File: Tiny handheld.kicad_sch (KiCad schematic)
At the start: 38 parts, among them J1 Conn_01x04_Female, J2 Conn_01x04_Female, J3 TYPE-C-31-M-12, U1 ATtiny85-20P, U2 ATtiny85-20M, U3 EEPROM-I2CEIAJ

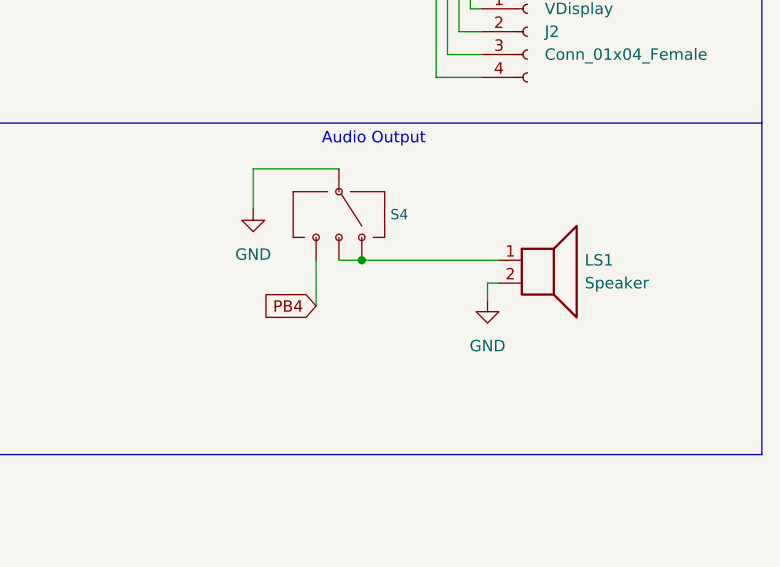
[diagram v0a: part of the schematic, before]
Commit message: changed switch for audio toggle
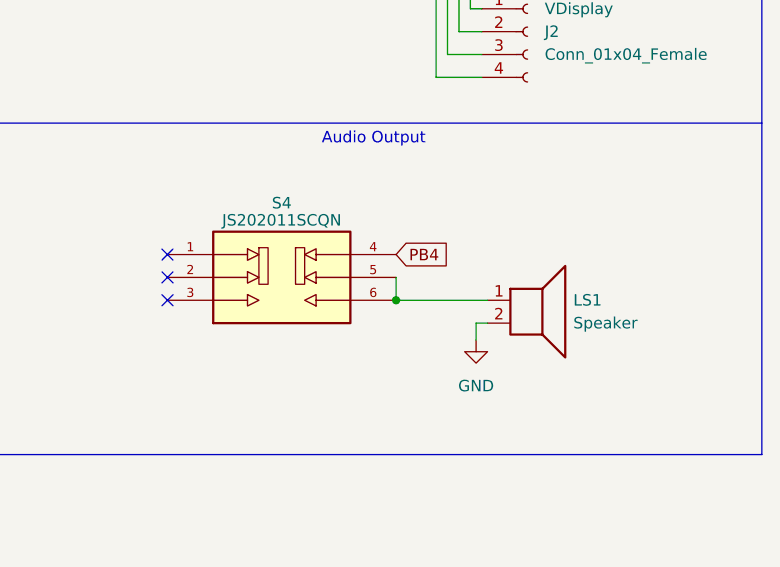
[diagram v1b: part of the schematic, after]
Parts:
- removed S4: SWITCH-SP3T-SMD, Snapeda:SW_JS202011SCQN, symbol SparkFun-Switches:SWITCH-SP3T-SMD
- added S4: JS202011SCQN, Snapeda:SW_JS202011SCQN, symbol JS202011SCQN:JS202011SCQN
- S3: footprint SnapEDA Library:SW_JS202011SCQN -> Snapeda:SW_JS202011SCQN
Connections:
- net PB4: now also S4.4
- net at LS1.1: now also S4.5, S4.6
- no-connect marks 2 -> 5
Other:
- moved on the sheet: LS1

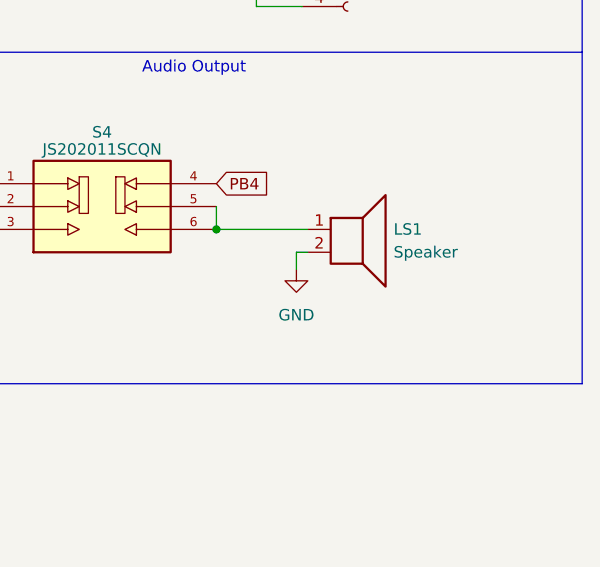
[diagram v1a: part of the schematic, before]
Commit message: changed speaker footprint and updated it
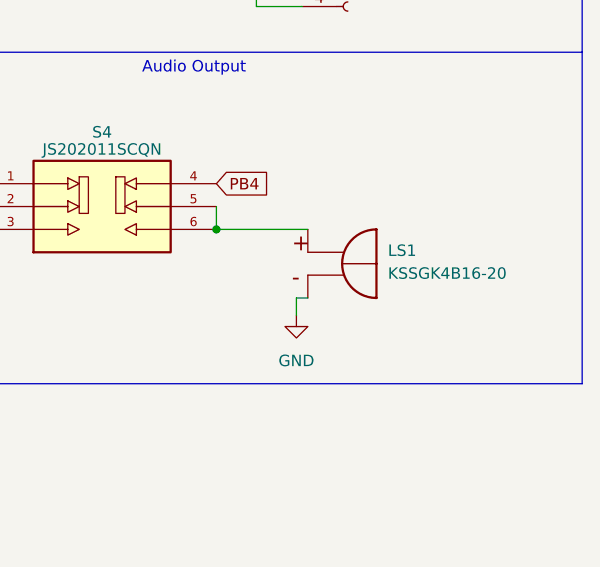
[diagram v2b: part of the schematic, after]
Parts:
- removed LS1: Speaker, Connector_PinHeader_2.54mm:PinHeader_1x02_P2.54mm_Vertical, symbol Device:Speaker
- added LS1: KSSGK4B16-20, Snapeda:XDCR_KSSGK4B16-20, symbol KSSGK4B16-20:KSSGK4B16-20
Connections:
- net GND: now also LS1.N
- net at S4.5, S4.6: now also LS1.P
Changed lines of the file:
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@@
     (stroke (width 0) (type default) (color 0 0 0 0))
   )
-  (wire (pts (xy 250.19 74.93) (xy 250.19 76.835))
+  (wire (pts (xy 250.19 80.01) (xy 250.19 81.915))
     (stroke (width 0) (type default) (color 0 0 0 0))
   )
@@
     (stroke (width 0) (type default) (color 0 0 0 0))
   )
-  (wire (pts (xy 251.46 74.93) (xy 250.19 74.93))
+  (wire (pts (xy 251.46 80.01) (xy 250.19 80.01))
     (stroke (width 0) (type default) (color 0 0 0 0))
   )
@@
     (pin "2")
   )
-  (symbol (lib_id "Device:Speaker") (at 256.54 72.39 0) (unit 1)
-    (in_bom yes) (on_board yes) (fields_autoplaced)
-    (property "Reference" "LS1" (id 0) (at 260.985 72.3899 0)
-      (effects (font (size 1.27 1.27)) (justify left))
-    )
-    (property "Value" "Speaker" (id 1) (at 260.985 74.9299 0)
-      (effects (font (size 1.27 1.27)) (justify left))
-    )
-    (property "Footprint" "Connector_PinHeader_2.54mm:PinHeader_1x02_P2.54mm_Vertical" (id 2) (at 256.54 77.47 0)
-      (effects (font (size 1.27 1.27)) hide)
-    )
-    (property "Datasheet" "~" (id 3) (at 256.286 73.66 0)
-      (effects (font (size 1.27 1.27)) hide)
-    )
-    (pin "1")
-    (pin "2")
-  )
   (symbol (lib_id "Device:D_Schottky") (at 50.8 100.33 180) (unit 1)
     (in_bom yes) (on_board yes)
@@
     (pin "4")
   )
-  (symbol (lib_id "power:GND") (at 250.19 76.835 0) (unit 1)
-    (in_bom yes) (on_board yes) (fields_autoplaced)
-    (property "Reference" "#PWR0110" (id 0) (at 250.19 83.185 0)
-      (effects (font (size 1.27 1.27)) hide)
-    )
-    (property "Value" "GND" (id 1) (at 250.19 81.915 0))
-    (property "Footprint" "" (id 2) (at 250.19 76.835 0)
-      (effects (font (size 1.27 1.27)) hide)
-    )
-    (property "Datasheet" "" (id 3) (at 250.19 76.835 0)
+  (symbol (lib_id "power:GND") (at 250.19 81.915 0) (unit 1)
+    (in_bom yes) (on_board yes) (fields_autoplaced)
+    (property "Reference" "#PWR0110" (id 0) (at 250.19 88.265 0)
+      (effects (font (size 1.27 1.27)) hide)
+    )
+    (property "Value" "GND" (id 1) (at 250.19 86.995 0))
+    (property "Footprint" "" (id 2) (at 250.19 81.915 0)
+      (effects (font (size 1.27 1.27)) hide)
+    )
+    (property "Datasheet" "" (id 3) (at 250.19 81.915 0)
       (effects (font (size 1.27 1.27)) hide)
     )
@@
     (pin "1")
   )
+  (symbol (lib_id "KSSGK4B16-20:KSSGK4B16-20") (at 254 77.47 0) (unit 1)
+    (in_bom yes) (on_board yes) (fields_autoplaced)
+    (property "Reference" "LS1" (id 0) (at 260.35 74.7487 0)
+      (effects (font (size 1.27 1.27)) (justify left))
+    )
+    (property "Value" "KSSGK4B16-20" (id 1) (at 260.35 77.2887 0)
+      (effects (font (size 1.27 1.27)) (justify left))
+    )
+    (property "Footprint" "Snapeda:XDCR_KSSGK4B16-20" (id 2) (at 254 77.47 0)
+      (effects (font (size 1.27 1.27)) (justify left bottom) hide)
+    )
+    (property "Datasheet" "" (id 3) (at 254 77.47 0)
+      (effects (font (size 1.27 1.27)) (justify left bottom) hide)
+    )
+    (property "STANDARD" "Manufacturer recommendations" (id 4) (at 254 77.47 0)
+      (effects (font (size 1.27 1.27)) (justify left bottom) hide)
+    )
+    (property "MAXIMUM_PACKAGE_HEIGHT" "2.2 mm" (id 5) (at 254 77.47 0)
+      (effects (font (size 1.27 1.27)) (justify left bottom) hide)
+    )
+    (property "MANUFACTURER" "Kingstate" (id 6) (at 254 77.47 0)
+      (effects (font (size 1.27 1.27)) (justify left bottom) hide)
+    )
+    (property "PARTREV" "1.1" (id 7) (at 254 77.47 0)
+      (effects (font (size 1.27 1.27)) (justify left bottom) hide)
+    )
+    (pin "N")
+    (pin "P")
+  )
   (symbol (lib_id "Device:C") (at 106.68 73.025 0) (unit 1)
     (in_bom yes) (on_board yes) (fields_autoplaced)
@@
       (reference "JP4") (unit 1) (value "SolderJumper_3_Bridged123") (footprint "Jumper:SolderJumper-3_P1.3mm_Open_RoundedPad1.0x1.5mm_NumberLabels")
     )
-    (path "/67918cda-4e84-4d93-8647-d5f18ad30e68"
-      (reference "LS1") (unit 1) (value "Speaker") (footprint "Connector_PinHeader_2.54mm:PinHeader_1x02_P2.54mm_Vertical")
+    (path "/e6505e47-bcf4-4c11-974c-950bd16fce03"
+      (reference "LS1") (unit 1) (value "KSSGK4B16-20") (footprint "Snapeda:XDCR_KSSGK4B16-20")
     )
     (path "/b3cf5acc-e257-462d-850a-8059d86079a1"

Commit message: first layout tryout
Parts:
- D1, D2, D3: footprint Diode_SMD:D_3220_8050Metric_Pad2.65x5.15mm_HandSolder -> Diode_SMD:D_1210_3225Metric_Pad1.42x2.65mm_HandSolder
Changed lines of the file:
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@@
       (effects (font (size 1.27 1.27)) (justify left))
     )
-    (property "Footprint" "Diode_SMD:D_3220_8050Metric_Pad2.65x5.15mm_HandSolder" (id 2) (at 56.515 134.62 0)
+    (property "Footprint" "Diode_SMD:D_1210_3225Metric_Pad1.42x2.65mm_HandSolder" (id 2) (at 56.515 134.62 0)
       (effects (font (size 1.27 1.27)) hide)
     )
@@
       (effects (font (size 1.27 1.27)) (justify left))
     )
-    (property "Footprint" "Diode_SMD:D_3220_8050Metric_Pad2.65x5.15mm_HandSolder" (id 2) (at 48.895 134.62 0)
+    (property "Footprint" "Diode_SMD:D_1210_3225Metric_Pad1.42x2.65mm_HandSolder" (id 2) (at 48.895 134.62 0)
       (effects (font (size 1.27 1.27)) hide)
     )
@@
     (property "Reference" "D1" (id 0) (at 50.8 102.87 0))
     (property "Value" "D_Schottky" (id 1) (at 53.975 97.155 0))
-    (property "Footprint" "Diode_SMD:D_3220_8050Metric_Pad2.65x5.15mm_HandSolder" (id 2) (at 50.8 100.33 0)
+    (property "Footprint" "Diode_SMD:D_1210_3225Metric_Pad1.42x2.65mm_HandSolder" (id 2) (at 50.8 100.33 0)
       (effects (font (size 1.27 1.27)) hide)
     )
@@
     )
     (path "/68f90c2a-7c7b-4d9c-8790-32721f4e1926"
-      (reference "D1") (unit 1) (value "D_Schottky") (footprint "Diode_SMD:D_3220_8050Metric_Pad2.65x5.15mm_HandSolder")
+      (reference "D1") (unit 1) (value "D_Schottky") (footprint "Diode_SMD:D_1210_3225Metric_Pad1.42x2.65mm_HandSolder")
     )
     (path "/5fd767ee-7166-48a9-a790-5eaffbe151cb"
-      (reference "D2") (unit 1) (value "3.6V") (footprint "Diode_SMD:D_3220_8050Metric_Pad2.65x5.15mm_HandSolder")
+      (reference "D2") (unit 1) (value "3.6V") (footprint "Diode_SMD:D_1210_3225Metric_Pad1.42x2.65mm_HandSolder")
     )
     (path "/3e1cd6ec-9057-4025-a95a-6564cb6c9ca0"
-      (reference "D3") (unit 1) (value "3.6V") (footprint "Diode_SMD:D_3220_8050Metric_Pad2.65x5.15mm_HandSolder")
+      (reference "D3") (unit 1) (value "3.6V") (footprint "Diode_SMD:D_1210_3225Metric_Pad1.42x2.65mm_HandSolder")
     )
     (path "/c820fea6-c141-491b-a697-ecc854c32ead"

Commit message: updated schematic (nothing special)
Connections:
- net PB0/SDA/MOSI: now also U1.5 (AREF/PB0), U2.11 (AREF/PB0)
- net PB1/MISO: now also U1.6 (PB1), U2.12 (PB1)
- net PB2/SCL/SCK: now also U1.7 (PB2), U2.14 (PB2)
- net PB3: now also U1.2 (XTAL1/PB3), U2.2 (XTAL1/PB3)
- net PB4: now also U1.3 (XTAL2/PB4), U2.5 (XTAL2/PB4)
- net PB5/RES: now also U1.1 (~{RESET}/PB5), U2.1 (~{RESET}/PB5)
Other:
- moved on the sheet: U1, U2
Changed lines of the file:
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@@
   (junction (at 43.18 83.185) (diameter 0) (color 0 0 0 0)
   )
-  (junction (at 160.655 35.56) (diameter 0) (color 0 0 0 0)
+  (junction (at 160.655 29.845) (diameter 0) (color 0 0 0 0)
+  )
+  (junction (at 160.655 34.925) (diameter 0) (color 0 0 0 0)
+  )
+  (junction (at 130.175 34.925) (diameter 0) (color 0 0 0 0)
   )
   (junction (at 53.34 83.185) (diameter 0) (color 0 0 0 0)
@@
   (junction (at 245.745 34.925) (diameter 0) (color 0 0 0 0)
   )
+  (junction (at 130.175 29.845) (diameter 0) (color 0 0 0 0)
+  )
   (junction (at 132.715 64.77) (diameter 0) (color 0 0 0 0)
   )
-  (junction (at 130.175 35.56) (diameter 0) (color 0 0 0 0)
-  )
   (junction (at 43.18 106.68) (diameter 0) (color 0 0 0 0)
   )
@@
   (junction (at 132.715 52.07) (diameter 0) (color 0 0 0 0)
   )
+  (junction (at 130.175 27.305) (diameter 0) (color 0 0 0 0)
+  )
   (junction (at 48.895 128.905) (diameter 0) (color 0 0 0 0)
   )
@@
   (junction (at 29.845 134.62) (diameter 0) (color 0 0 0 0)
   )
+  (junction (at 160.655 27.305) (diameter 0) (color 0 0 0 0)
+  )
   (junction (at 42.545 116.84) (diameter 0) (color 0 0 0 0)
   )
@@
   (junction (at 164.465 32.385) (diameter 0) (color 0 0 0 0)
   )
-  (junction (at 128.905 107.315) (diameter 0) (color 0 0 0 0)
+  (junction (at 160.655 32.385) (diameter 0) (color 0 0 0 0)
   )
   (junction (at 160.655 49.53) (diameter 0) (color 0 0 0 0)
@@
   (junction (at 53.34 50.165) (diameter 0) (color 0 0 0 0)
   )
-  (junction (at 36.83 22.225) (diameter 0) (color 0 0 0 0)
-  )
   (junction (at 42.545 114.3) (diameter 0) (color 0 0 0 0)
   )
@@
   )
   (junction (at 247.015 32.385) (diameter 0) (color 0 0 0 0)
+  )
+  (junction (at 130.175 32.385) (diameter 0) (color 0 0 0 0)
   )
   (junction (at 132.715 49.53) (diameter 0) (color 0 0 0 0)
@@
     (stroke (width 0) (type default) (color 0 0 0 0))
   )
-  (wire (pts (xy 160.655 35.56) (xy 160.655 43.18))
+  (wire (pts (xy 160.655 34.925) (xy 160.655 43.18))
     (stroke (width 0) (type default) (color 0 0 0 0))
   )
@@
     (stroke (width 0) (type default) (color 0 0 0 0))
   )
-  (wire (pts (xy 130.175 35.56) (xy 130.175 45.72))
+  (wire (pts (xy 130.175 34.925) (xy 130.175 45.72))
     (stroke (width 0) (type default) (color 0 0 0 0))
   )
@@
     (stroke (width 0) (type default) (color 0 0 0 0))
   )
-  (wire (pts (xy 160.655 34.925) (xy 160.655 35.56))
-    (stroke (width 0) (type default) (color 0 0 0 0))
-  )
   (wire (pts (xy 165.735 64.77) (xy 167.005 64.77))
     (stroke (width 0) (type default) (color 0 0 0 0))
@@
   )
   (wire (pts (xy 97.155 113.665) (xy 97.155 107.315))
-    (stroke (width 0) (type default) (color 0 0 0 0))
-  )
-  (wire (pts (xy 130.175 34.925) (xy 130.175 35.56))
     (stroke (width 0) (type default) (color 0 0 0 0))
   )
@@
     )
   )
+  (global_label "VCC" (shape input) (at 36.83 22.225 90) (fields_autoplaced)
+    (effects (font (size 1.27 1.27)) (justify left))
+    (property "Intersheet References" "${INTERSHEET_REFS}" (id 0) (at 36.7506 16.1833 90)
+      (effects (font (size 1.27 1.27)) (justify left) hide)
+    )
+  )
   (global_label "PB5{slash}RES" (shape input) (at 118.745 27.305 180) (fields_autoplaced)
     (effects (font (size 1.27 1.27)) (justify right))
@@
     (effects (font (size 1.27 1.27)) (justify left))
     (property "Intersheet References" "${INTERSHEET_REFS}" (id 0) (at 84.9026 34.8456 0)
+      (effects (font (size 1.27 1.27)) (justify left) hide)
+    )
+  )
+  (global_label "VCC" (shape input) (at 128.905 107.315 0) (fields_autoplaced)
+    (effects (font (size 1.27 1.27)) (justify left))
+    (property "Intersheet References" "${INTERSHEET_REFS}" (id 0) (at 134.9467 107.2356 0)
       (effects (font (size 1.27 1.27)) (justify left) hide)
     )
@@
     (pin "2")
   )
-  (symbol (lib_id "MCU_Microchip_ATtiny:ATtiny85-20P") (at 145.415 34.29 0) (unit 1)
-    (in_bom yes) (on_board yes)
-    (property "Reference" "U1" (id 0) (at 140.97 22.225 0)
+  (symbol (lib_id "MCU_Microchip_ATtiny:ATtiny85-20P") (at 145.415 33.655 0) (unit 1)
+    (in_bom yes) (on_board yes)
+    (property "Reference" "U1" (id 0) (at 140.97 21.59 0)
       (effects (font (size 1.27 1.27)) (justify right))
     )
-    (property "Value" "ATtiny85-20P" (id 1) (at 144.78 24.13 0)
+    (property "Value" "ATtiny85-20P" (id 1) (at 144.78 23.495 0)
       (effects (font (size 1.27 1.27)) (justify right))
     )
-    (property "Footprint" "Package_DIP:DIP-8_W7.62mm" (id 2) (at 147.32 62.23 0)
+    (property "Footprint" "Package_DIP:DIP-8_W7.62mm" (id 2) (at 147.32 61.595 0)
       (effects (font (size 1.27 1.27) italic) hide)
     )
-    (property "Datasheet" "http://ww1.microchip.com/downloads/en/DeviceDoc/atmel-2586-avr-8-bit-microcontroller-attiny25-attiny45-attiny85_datasheet.pdf" (id 3) (at 160.02 58.42 0)
+    (property "Datasheet" "http://ww1.microchip.com/downloads/en/DeviceDoc/atmel-2586-avr-8-bit-microcontroller-attiny25-attiny45-attiny85_datasheet.pdf" (id 3) (at 160.02 57.785 0)
       (effects (font (size 1.27 1.27)) hide)
     )
@@
     (pin "1")
   )
-  (symbol (lib_id "power:VCC") (at 128.905 107.315 0) (unit 1)
-    (in_bom yes) (on_board yes) (fields_autoplaced)
-    (property "Reference" "#PWR0105" (id 0) (at 128.905 111.125 0)
-      (effects (font (size 1.27 1.27)) hide)
-    )
-    (property "Value" "VCC" (id 1) (at 128.905 102.235 0))
-    (property "Footprint" "" (id 2) (at 128.905 107.315 0)
-      (effects (font (size 1.27 1.27)) hide)
-    )
-    (property "Datasheet" "" (id 3) (at 128.905 107.315 0)
-      (effects (font (size 1.27 1.27)) hide)
-    )
-    (pin "1")
-  )
   (symbol (lib_id "Device:R") (at 43.18 53.975 0) (unit 1)
     (in_bom yes) (on_board yes) (fields_autoplaced)
@@
     (pin "2")
   )
-  (symbol (lib_id "power:VCC") (at 36.83 22.225 0) (unit 1)
-    (in_bom yes) (on_board yes) (fields_autoplaced)
-    (property "Reference" "#PWR0109" (id 0) (at 36.83 26.035 0)
-      (effects (font (size 1.27 1.27)) hide)
-    )
-    (property "Value" "VCC" (id 1) (at 36.83 17.145 0))
-    (property "Footprint" "" (id 2) (at 36.83 22.225 0)
-      (effects (font (size 1.27 1.27)) hide)
-    )
-    (property "Datasheet" "" (id 3) (at 36.83 22.225 0)
-      (effects (font (size 1.27 1.27)) hide)
-    )
-    (pin "1")
-  )
   (symbol (lib_id "power:PWR_FLAG") (at 43.18 106.68 0) (unit 1)
     (in_bom yes) (on_board yes) (fields_autoplaced)
@@
     (pin "4")
   )
-  (symbol (lib_id "MCU_Microchip_ATtiny:ATtiny85-20M") (at 145.415 41.91 0) (unit 1)
-    (in_bom yes) (on_board yes)
-    (property "Reference" "U2" (id 0) (at 153.035 22.225 0)
+  (symbol (lib_id "MCU_Microchip_ATtiny:ATtiny85-20M") (at 145.415 41.275 0) (unit 1)
+    (in_bom yes) (on_board yes)
+    (property "Reference" "U2" (id 0) (at 153.035 21.59 0)
       (effects (font (size 1.27 1.27)) (justify right))
     )
-    (property "Value" "ATtiny85-20M" (id 1) (at 161.29 24.13 0)
+    (property "Value" "ATtiny85-20M" (id 1) (at 161.29 23.495 0)
       (effects (font (size 1.27 1.27)) (justify right))
     )
-    (property "Footprint" "Snapeda:QFN50P400X400X80-21N" (id 2) (at 156.21 45.085 0)
+    (property "Footprint" "Snapeda:QFN50P400X400X80-21N" (id 2) (at 156.21 44.45 0)
       (effects (font (size 1.27 1.27) italic) hide)
     )
-    (property "Datasheet" "http://ww1.microchip.com/downloads/en/DeviceDoc/atmel-2586-avr-8-bit-microcontroller-attiny25-attiny45-attiny85_datasheet.pdf" (id 3) (at 186.055 42.545 0)
+    (property "Datasheet" "http://ww1.microchip.com/downloads/en/DeviceDoc/atmel-2586-avr-8-bit-microcontroller-attiny25-attiny45-attiny85_datasheet.pdf" (id 3) (at 186.055 41.91 0)
       (effects (font (size 1.27 1.27)) hide)
     )
@@
       (reference "#PWR0104") (unit 1) (value "GND") (footprint "")
     )
-    (path "/8f597b01-b914-42f9-803c-9063988abc27"
-      (reference "#PWR0105") (unit 1) (value "VCC") (footprint "")
-    )
     (path "/ef165256-f975-442e-8a79-6b8715d4b315"
       (reference "#PWR0106") (unit 1) (value "GND") (footprint "")
@@
       (reference "#PWR0108") (unit 1) (value "VCC") (footprint "")
     )
-    (path "/b7b686cb-da0a-46af-a6c0-01b14bd7cfd8"
-      (reference "#PWR0109") (unit 1) (value "VCC") (footprint "")
-    )
     (path "/a1137bda-e367-49f0-a939-560fc952dcc4"
